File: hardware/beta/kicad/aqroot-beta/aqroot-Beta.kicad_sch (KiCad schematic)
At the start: 0 parts

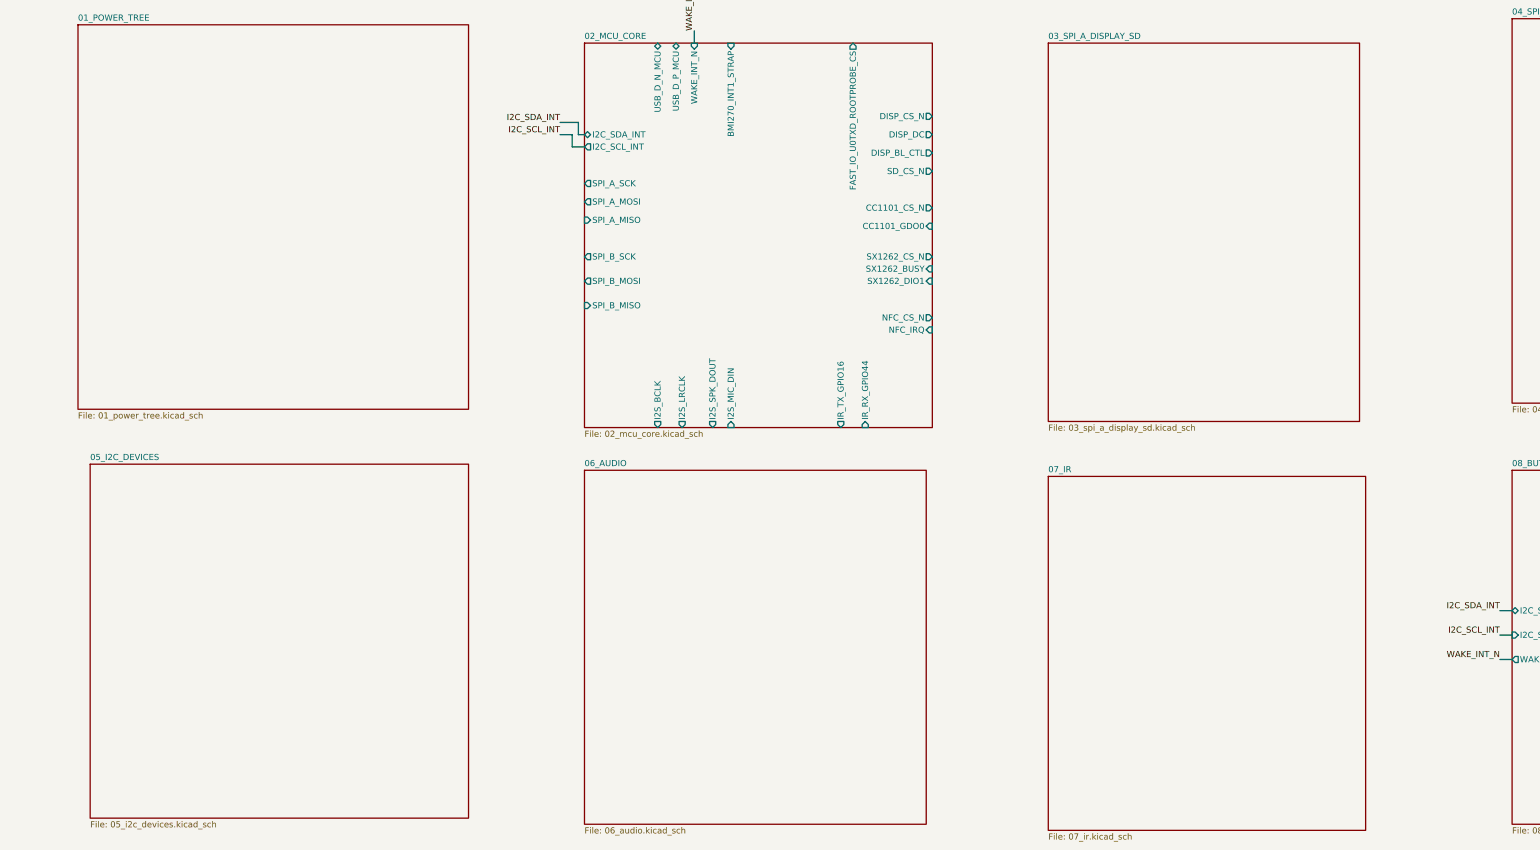
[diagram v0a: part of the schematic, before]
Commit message: AQROOT Beta: capture I2C, audio, IR, and SPI-A subsystems
Reconciles the active KiCad project from OneDrive into the canonical
repository. The four subsystem sheets existed here only as 169-byte
empty stubs; the real schematic capture had been done in the OneDrive
working copy.

Sheets brought in:
  03_spi_a_display_sd.kicad_sch   stub ->  62136 bytes
  05_i2c_devices.kicad_sch        stub ->  59631 bytes
  06_audio.kicad_sch              stub ->  55263 bytes
  07_ir.kicad_sch                 stub ->  50216 bytes

Also updated: aqroot-Beta.kicad_sch (root sheet, now carrying the
child sheet instances) and aqroot-Beta.kicad_pro.

03_spi_a_display_sd instantiates AQROOT_Beta:ILI9341_FT6236_MODULE_-
PLACEHOLDER; its cached symbol matches libraries/AQROOT_Beta.kicad_sym
exactly (13 pins, blank footprint, on_board=no).

Deliberately not taken from OneDrive:
  - sym-lib-table / fp-lib-table. The OneDrive copies hard-code an
    absolute P:/ path to this repository's library; the versions kept
    here use ${KIPRJMOD} and stay portable.
  - aqroot-Beta.kicad_prl (local project state) and .history/
    (2388 editor-history files, 5.87 MB).

Sheets identical on both sides and therefore untouched: 01_power_tree,
02_mcu_core, 04_spi_b_radios_nfc, 08_buttons_expanders,
09_community_header, aqroot-Beta.kicad_pcb.

Every copied file was verified by SHA-256 against its source, and each
staged blob is byte-identical to the working-tree file: CRLF endings
are preserved per .gitattributes, with no EOL normalization or
reformatting.

Co-Authored-By: Claude Opus 5 <noreply@anthropic.com>
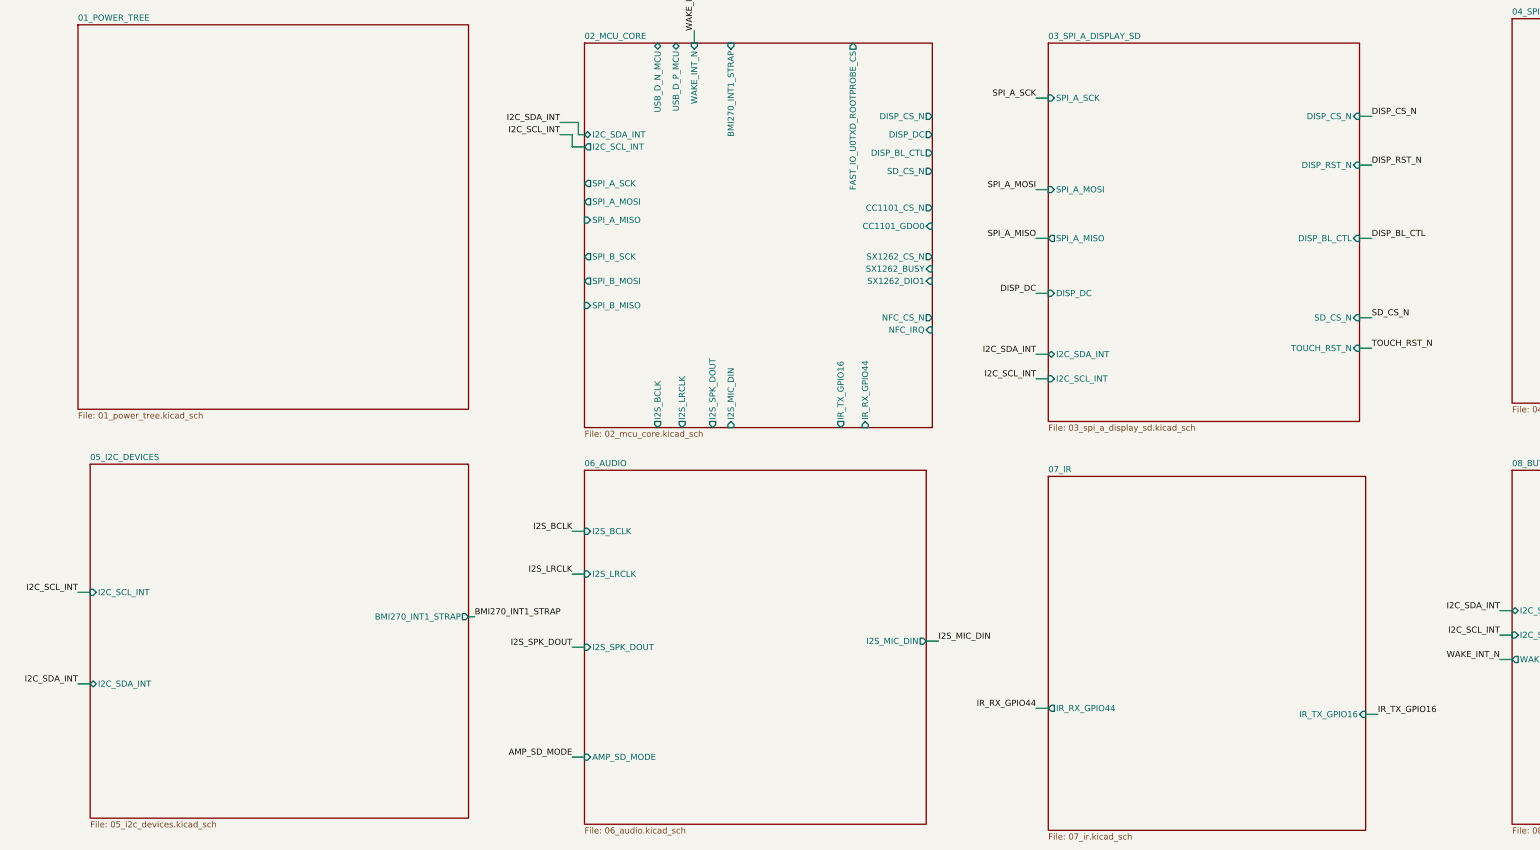
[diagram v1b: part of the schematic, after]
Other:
- sheet 03_SPI_A_DISPLAY_SD ports: added DISP_BL_CTL, DISP_CS_N, DISP_DC, DISP_RST_N, I2C_SCL_INT, I2C_SDA_INT, SD_CS_N, SPI_A_MISO, SPI_A_MOSI, SPI_A_SCK, TOUCH_RST_N; removed none
- sheet 05_I2C_DEVICES ports: added BMI270_INT1_STRAP, I2C_SCL_INT, I2C_SDA_INT; removed none
- sheet 06_AUDIO ports: added AMP_SD_MODE, I2S_BCLK, I2S_LRCLK, I2S_MIC_DIN, I2S_SPK_DOUT; removed none
- sheet 07_IR ports: added IR_RX_GPIO44, IR_TX_GPIO16; removed none

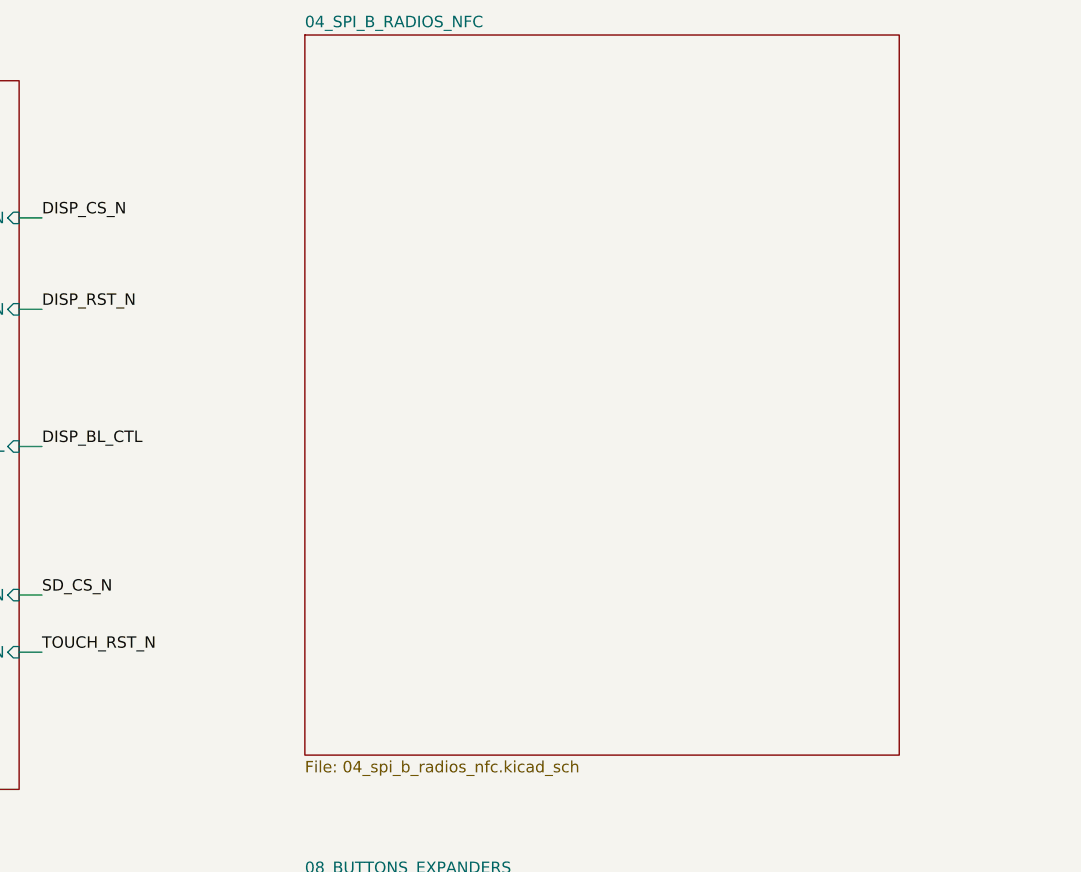
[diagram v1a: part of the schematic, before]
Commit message: AQROOT Beta: capture SPI-B radios and NFC architecture
Completes sheet 04, bringing all three SPI Bus B devices into the
schematic against the functional placeholder symbols added in 5e4471a,
ba2be78 and 1f152bd. Bus B is now the shared SPI_B_SCK / SPI_B_MOSI /
SPI_B_MISO bus with one chip select per device.

CC1101 -- AQROOT_Beta:CC1101_RADIO_PLACEHOLDER
  CC1101_CS_N, CC1101_GDO0, CC1101_RF_TBD, 100nF decoupling,
  10k hardware pull-up on CC1101_CS_N.

SX1262 -- AQROOT_Beta:SX1262_MODULE_PLACEHOLDER
  SX1262_CS_N, SX1262_BUSY, SX1262_DIO1, SX1262_RST_N (from expander
  U60 P01), SX1262_RF_TBD, 100nF decoupling, 10k hardware pull-up on
  SX1262_CS_N.

ST25R3916 -- AQROOT_Beta:ST25R3916_NFC_PLACEHOLDER
  VDD_IO_3V3 and VDD_DIG_3V3 to +3V3, VDD_PA_5V to NFC_5V_PA_PENDING
  (the switched 5V PA rail, boost IC unresolved). NFC_CS_N, NFC_IRQ,
  and the RF and clock ports NFC_RFO1/RFO2/RFI1/RFI2_TBD and
  NFC_XIN/XOUT_TBD. 10k hardware pull-up on NFC_CS_N, plus provisional
  100nF placeholders on +3V3 and on NFC_5V_PA_PENDING.

Passives placed: C16, C17 (100nF), C18, C19 (100nF_PLACEHOLDER),
R27, R28, R29 (10k CS pull-ups).

Root sheet exposes and labels SPI_B_SCK, SPI_B_MOSI, SPI_B_MISO,
CC1101_CS_N, CC1101_GDO0, SX1262_CS_N, SX1262_BUSY, SX1262_DIO1,
SX1262_RST_N, NFC_CS_N and NFC_IRQ.

All three parts carry a blank Footprint and on_board=no, and the sheet
carries DO NOT ROUTE notes. Nothing here is routable: the CC1101
module-vs-bare-IC choice, the SX1262 certified module (Ebyte E22 vs
Waveshare Core1262), and the ST25R3916 package, support networks, coil
and matching all remain unresolved. Every _TBD and _PENDING net name is
deliberate and must be replaced before layout.

Also in this commit, both rewritten by KiCad during the same session:
  - aqroot-Beta.kicad_pro: ERC pin_to_pin severity raised from warning
    to error, and used_designators updated by the annotator.
  - 03_spi_a_display_sd.kicad_sch: two pin UUIDs regenerated on save;
    no connectivity or compon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
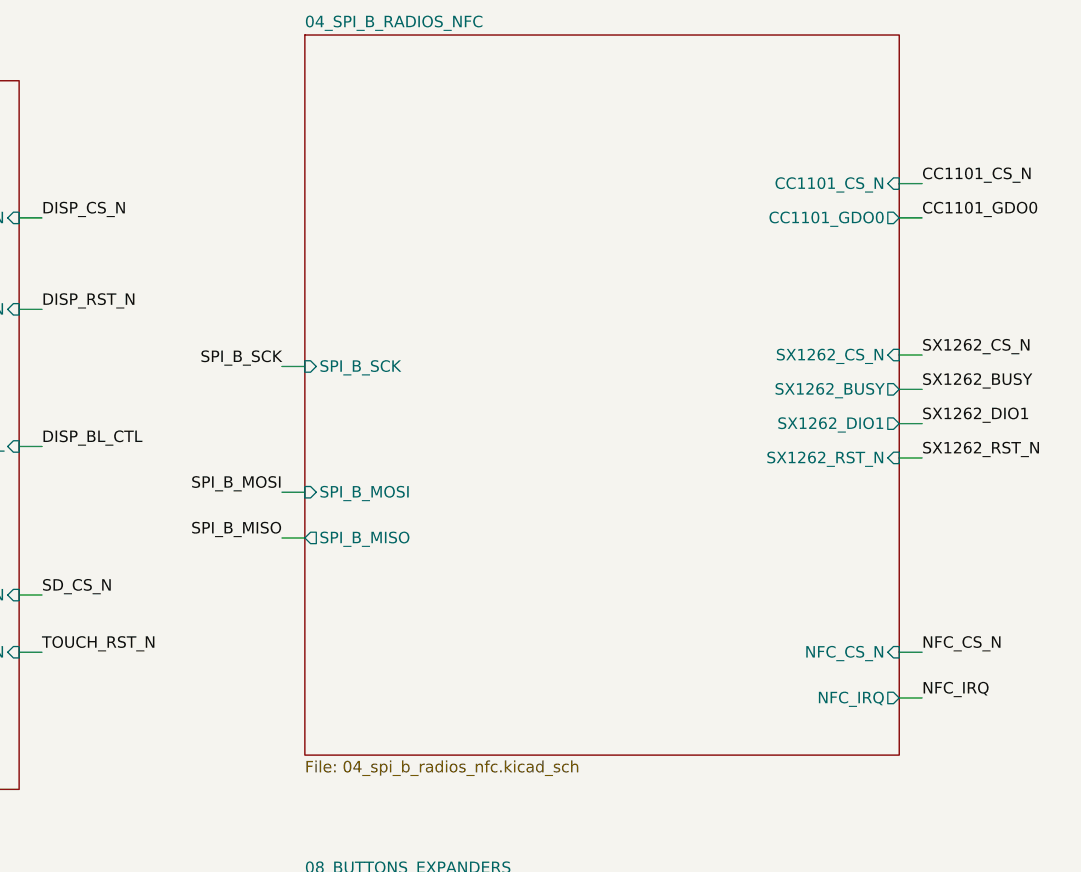
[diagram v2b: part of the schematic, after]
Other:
- sheet 04_SPI_B_RADIOS_NFC ports: added CC1101_CS_N, CC1101_GDO0, NFC_CS_N, NFC_IRQ, SPI_B_MISO, SPI_B_MOSI, SPI_B_SCK, SX1262_BUSY, SX1262_CS_N, SX1262_DIO1, SX1262_RST_N; removed none
